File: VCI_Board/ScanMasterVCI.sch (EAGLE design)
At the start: 73 parts, among them IC1 XMEGA16A4A, IC2 LTC3631, IC3 LM317MDT, IC4 SN74AHCT1G04, IC5 SN74AHCT1G04, IC6 TL331, IC7 74AHCT1G32DBV, IC8 SN74AHCT1G04, IC9 SN74AHCT1G04, Q1 MMBT4403LT1SMD, Q2 MMBT4403LT1SMD, Q3 MMBT4403LT1SMD, Q5 PZT3904, Q6 MMBT3904, Q8 MMBT3904/SOT, U2 LM339MA, U3 MAX17502EATB+T, U4 MAX13444EASA+

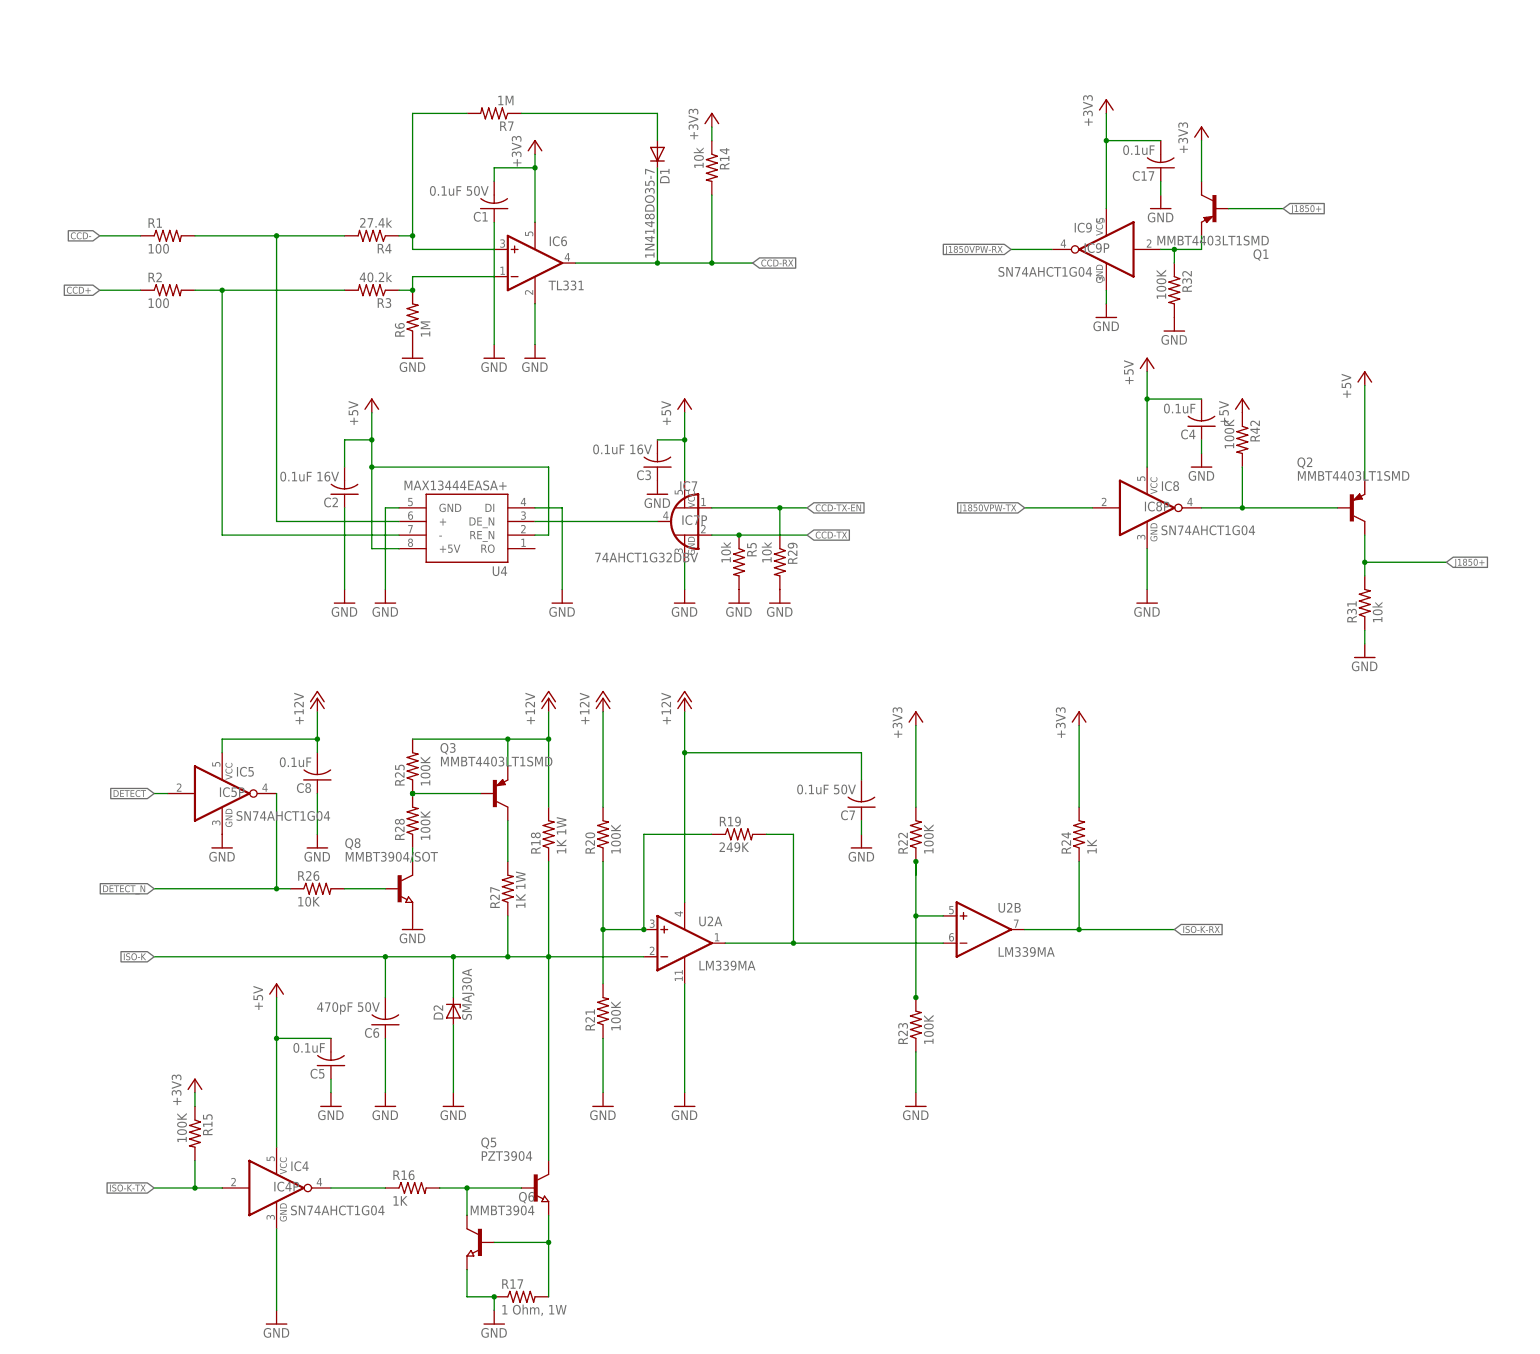
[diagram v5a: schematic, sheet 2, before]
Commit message: Started the work of simplifying the J1850VPW and ISO9141 circuitry.
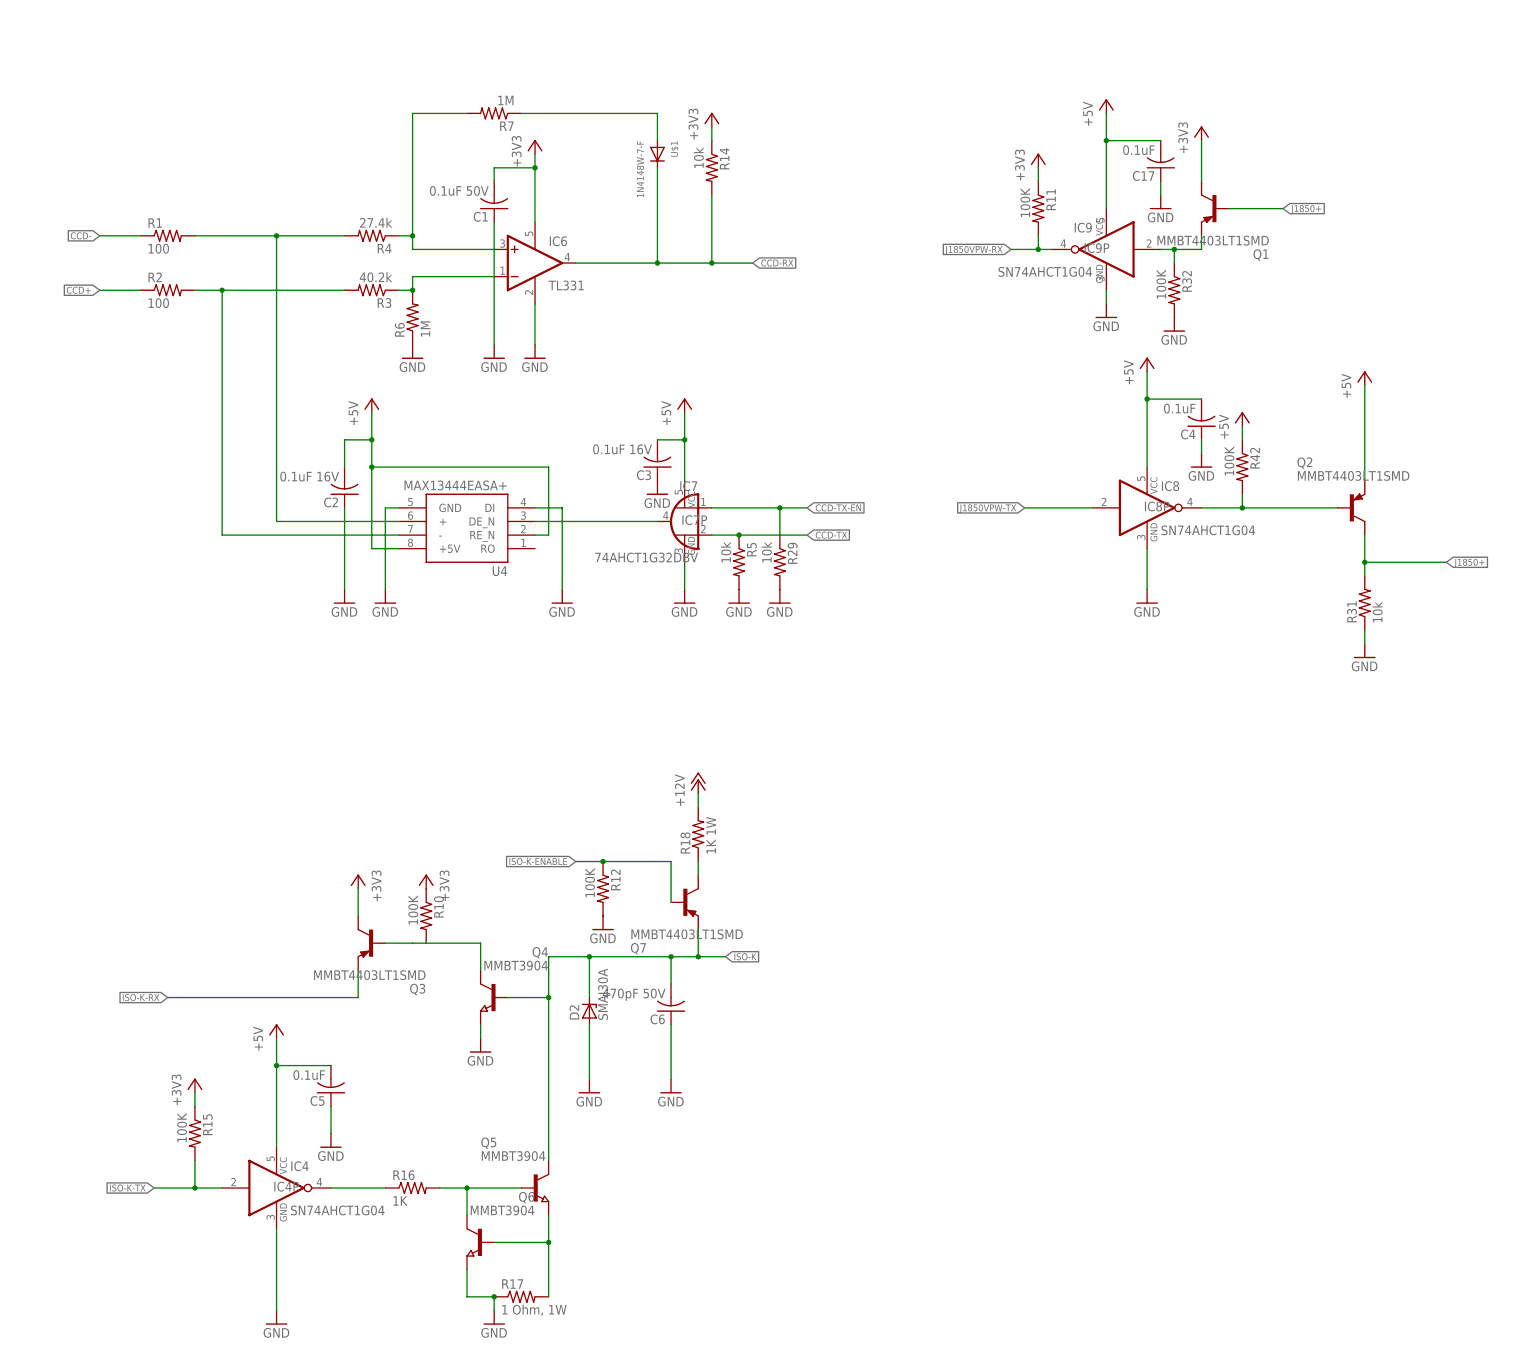
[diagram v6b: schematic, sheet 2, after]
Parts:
- removed C13: 4.7uF 35V, adafruit:C-USC0805
- removed C14, C15, C7: 0.1uF 50V, adafruit:C-USC0805
- removed C16: 1uF 16V, adafruit:C-USC0805
- removed C8: 0.1uF, adafruit:C-USC0805
- removed D1: 1N4148DO35-7, diode:1N4148DO35-7
- removed IC2: LTC3631, customics:LTC3631
- removed IC3: LM317MDT, customics:LM317MDT
- removed IC5: SN74AHCT1G04, 74xx-little-us:74AHC1G04DBV
- removed L2: 100uH, inductor-neosid:MS50
- removed Q8: MMBT3904/SOT, semicon-smd-ipc:NPN-TRANSISTOR_SOT23
- removed R13: 210 1%, adafruit:R-US_R0805
- removed R19: 249K, adafruit:R-US_R0805W
- removed R20, R21, R22, R23, R25, R28: 100K, adafruit:R-US_R0805W
- removed R24: 1K, adafruit:R-US_R0805W
- removed R26: 10K, adafruit:R-US_R0805W
- removed R27: 1K 1W, adafruit:R-US_R0805W
- removed U2: LM339MA, linear:AD8684R
- added Q4: MMBT3904, semicon-smd-ipc:NPN-TRANSISTOR_SOT23
- added Q7: MMBT4403LT1SMD, transistor-pnp:MMBT4403LT1SMD
- added U$1: 1N4148W-7-F, customics:1N4148W-7-F
- added U1: MAX17502FATB+T, customics:MAX17502EATB+
- Q5: value PZT3904 -> MMBT3904
- R10: value 2.67M 1% -> 100K; device adafruit:R-US_R0805 -> adafruit:R-US_R0805W
- R11: value 110k 1% -> 100K; device adafruit:R-US_R0805 -> adafruit:R-US_R0805W
- R12: value 1.33k 1% -> 100K; device adafruit:R-US_R0805 -> adafruit:R-US_R0805W
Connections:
- removed net CBV: C13.2, C14.2, IC3.VIN, L2.2, R10.2
- removed net DETECT: IC1.PD0, IC5A.I
- removed net DETECT_N: IC1.PD1, IC5A.O, R26.1
- removed net J1850VPW: IC1.PC4
- removed net J1850VPW-PWR: C16.2, IC3.VOUT, R13.2
- removed net N$18: R19.1, R20.1, R21.2, U2A.+IN
- removed net N$19: R22.1, R23.2, U2B.+IN
- removed net N$20: Q3.B, R25.1, R28.2
- removed net N$21: Q8.C, R28.1
- removed net N$22: Q8.B, R26.2
- removed net N$23: Q3.C, R27.2
- removed net N$24: IC3.ADJ, R12.2, R13.1
- new net ISO-K-ENABLE: IC1.PD4, Q7.B, R12.1
- net +12V: no longer C15.2, C7.2, C8.2, IC2.RUN, IC2.VIN, IC5P.VCC, Q3.E, R20.2, R25.2, U2P.V+
- net +3V3: now also Q3.C, R10.1, R11.1; no longer C17.2, IC9P.VCC, R22.2, R24.2
- net +5V: now also C17.2, IC9P.VCC
- net CCD-RX: now also U$1.C; no longer D1.C
- net GND: now also Q4.E, R12.2; no longer C13.1, C14.1, C15.1, C16.1, C7.1, C8.1, IC2.GND, IC2.ISET, IC5P.GND, Q8.E, R11.1, R12.1, R21.1, R23.1, U2P.V-
- net ISO-K: now also Q4.B, Q7.E; no longer R18.1, R27.1, U2A.-IN
- net ISO-K-RX: now also Q3.E; no longer R24.1, U2B.OUT
- net J1850VPW-RX: now also IC1.PC4, R11.2
- net J1850VPW-TX: now also IC1.PC5
- net N$10: now also IC1.PD5; no longer IC2.VFB, R10.1, R11.2
- net N$13: now also Q3.B, Q4.C, R10.2; no longer IC2.SW, L2.1
- net N$17: now also Q7.C, R18.1; no longer R19.2, U2A.OUT, U2B.-IN
- net N$3: now also U$1.A; no longer D1.A
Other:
- moved on the sheet: C5, C6, D2, Q3, R18, R42

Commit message: Added SCI RX/TX circuits. Added +5V. Added filtered battery voltage circuit. Added transistors to SCI pins for rudimentary multiplexing. Removed ISO9141 circuitry in favor of an off-the-shelf LIN controller.
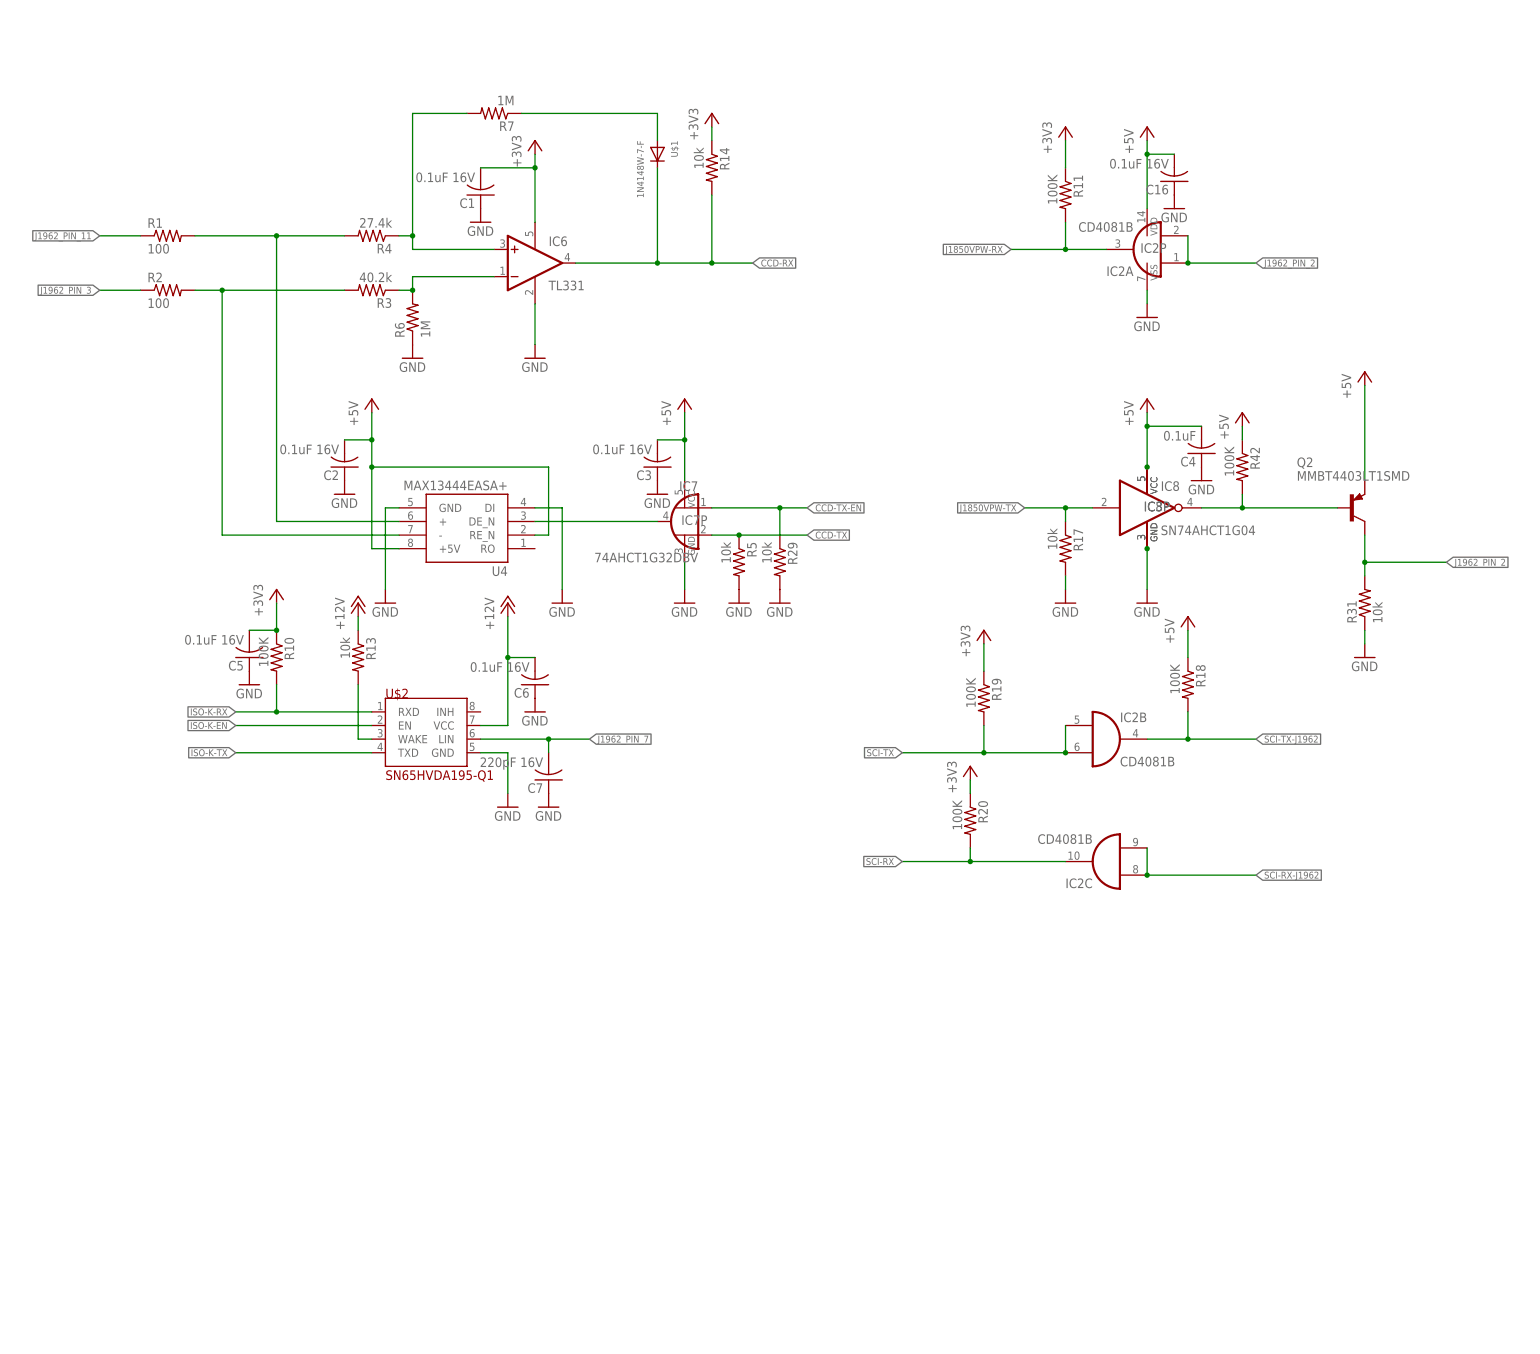
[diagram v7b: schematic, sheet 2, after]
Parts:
- removed IC9: SN74AHCT1G04, 74xx-little-us:74AHC1G04DBV
- removed R32: 100K, adafruit:R-US_R0805W
- added C13: 1uF, adafruit:C-USC0805
- added C14: 3300pF, adafruit:C-USC0805
- added C15: 22uF, adafruit:C-USC0805
- added C16: 0.1uF 16V, adafruit:C-USC0805
- added C18: 100uF, adafruit:C-USC0805
- added C19: 330pF, adafruit:C-USC0805
- added C20: 0.1uF, adafruit:C-USC0805
- added C7: 220pF 16V, adafruit:C-USC0805
- added C8: 2.2uF 100V, adafruit:C-USC0805
- added D1: SMAJ5.0A, diode:ZENER-DIODESMB
- added D3: MM5Z10V, diode:DIODE-SOD523
- added IC2: CD4081B, 40xx:4081D
- added IC3: SN74AHCT1G04, 74xx-little-us:74AHC1G04DBV
- added L2: 15uH, inductor-neosid:MS50
- added L3: 22uH, inductor-neosid:MS50
- added Q8, Q9: MMBT4403, transistor-pnp:MMBT4403LT1SMD
- added R13: 10k, adafruit:R-US_R0805
- added R19, R20, R21, R24, R25, R26, R27: 100K, adafruit:R-US_R0805W
- added R22: 200k, adafruit:R-US_R0805
- added R23: 20k, adafruit:R-US_R0805
- added U$2: SN65HVDA195-Q1, customics:SN65HVDA195-Q1
- added U$3: ZXMP6A17G, customics:ZXMP6A17G
- C1: value 0.1uF 50V -> 0.1uF 16V
- C5: value 0.1uF -> 0.1uF 16V
- C6: value 470pF 50V -> 0.1uF 16V
- D2: value SMAJ30A -> 1.5SMC43AT3G; device diode:ZENER-DIODEZD-2.5 -> diode:ZENER-DIODESMB
- Q1, Q3, Q7: value MMBT4403LT1SMD -> MMBT4403
- Q6: value MMBT3904 -> MMBT4403; device semicon-smd-ipc:NPN-TRANSISTOR_SOT23 -> transistor-pnp:MMBT4403LT1SMD
- R15: value 100K -> 866k 1%; device adafruit:R-US_R0805W -> adafruit:R-US_R0805
- R16: value 1K -> 3.32M 1%; device adafruit:R-US_R0805W -> adafruit:R-US_R0805
- R17: value 1 Ohm, 1W -> 10k; device adafruit:R-US_R0805W -> adafruit:R-US_R0805
- R18: value 1K 1W -> 100K
- U1: value MAX17502FATB+T -> MAX17502FATB+
- U3: value MAX17502EATB+T -> MAX17502EATB+
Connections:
- net CCD+ renamed J1962_PIN_3
- net CCD- renamed J1962_PIN_11
- removed net ISO-K: C6.2, D2.C, Q4.B, Q5.C, Q7.E
- removed net ISO-K-ENABLE: IC1.PD4, Q7.B, R12.1
- removed net J1850+: Q1.B, Q2.C, R31.2
- removed net N$10: IC1.PD5
- removed net N$26: IC9A.I, Q1.E, R32.1
- new net ISO-K-EN: IC1.PD4, U$2.EN
- new net J1962_PIN_12: Q8.C, R27.2
- new net J1962_PIN_14: Q9.C, R25.2
- new net J1962_PIN_2: IC2A.I0, IC2A.I1, Q2.C, R31.2
- new net J1962_PIN_6: Q6.C, R24.2
- new net J1962_PIN_7: C7.2, Q1.E, Q3.E, Q4.C, Q5.C, U$2.LIN
- new net J1962_PIN_9: Q7.C, R26.2
- new net N$18: C17.2, L3.1, U$3.D
- new net N$19: L2.1, U1.LX
- new net N$20: D3.A, R22.1, R23.2, U$3.G
- new net N$21: Q4.E, R21.2
- new net N$22: IC1.PD6
- new net SCI-RX-J1962: IC2C.I0, IC2C.I1, Q1.C, Q3.C
- new net SCI-TX-J1962: IC2B.O, Q6.E, Q7.E, Q8.E, Q9.E, R18.2
- new net SCI_RX_PIN_15_EN: IC1.PD5, IC4A.I, Q1.B, Q5.B
- new net SCI_RX_PIN_15_EN_INV: IC4A.O, Q3.B, Q4.B
- new net SCI_TX_PIN_12_EN: Q8.B
- new net SCI_TX_PIN_14_EN: Q9.B
- new net SCI_TX_PIN_6_EN: Q6.B
- new net SCI_TX_PIN_9_EN: Q7.B
- new net VBAT: D2.C, D3.C, R22.2, U$3.S
- net +12V: now also C18.2, C19.2, C6.2, C8.2, L3.2, R13.1, R16.2, U$2.VCC, U1.VIN, U3.VIN; no longer R18.2, U3.+12V
- net +3V3: now also C5.2, R19.1, R20.1; no longer Q1.C, Q3.C, R15.1
- net +5V: now also C15.2, C16.2, C20.2, D1.C, IC2P.VDD, IC3P.VCC, L2.2, R12.1, R18.1, R21.1, U1.FB_VO; no longer C17.2, C5.2, IC9P.VCC
- net GND: now also C13.1, C14.1, C15.1, C16.1, C18.1, C19.1, C20.1, C7.1, C8.1, D1.A, IC2P.VSS, IC3P.GND, R15.1, R17.2, R23.1, R24.1, R25.1, R26.1, R27.1, U$2.GND, U1.GND, U1.PGND; no longer IC9P.GND, Q4.E, Q6.E, R12.2, R17.1, R32.2
- net ISO-K-RX: now also R10.2, U$2.RXD; no longer Q3.E
- net ISO-K-TX: now also U$2.TXD; no longer IC4A.I, R15.2
- net J1850VPW-RX: now also IC2A.O; no longer IC9A.O
- net J1850VPW-TX: now also R17.1
- net N$13: now also Q5.E, R12.2; no longer Q3.B, Q4.C, R10.2
- net N$14: now also R13.2, U$2.WAKE; no longer IC4A.O, R16.1
- net N$15: now also C13.2, U1.VCC; no longer Q5.B, Q6.C, R16.2
- net N$16: now also R15.2, R16.1, U1.EN_UVLO; no longer Q5.E, Q6.B, R17.2
- net N$17: now also C14.2, U1.SS; no longer Q7.C, R18.1
- net SCI-RX: now also IC2C.O, R20.2
- net SCI-TX: now also IC2B.I0, IC2B.I1, R19.2
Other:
- note added: "Battery Volts (Filtered)"
- note added: "Filtered Battery Volts -> +3.3V"
- note added: "Filtered Battery Volts -> +5V"
- moved on the sheet: C1, C2, C4, C5, C6, D5, R10, R11, R17, R18, U1
